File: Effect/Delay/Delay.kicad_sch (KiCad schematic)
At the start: 23 parts, among them J1 Conn_01x04_Pin, J2 Conn_01x03_Pin, U1 PT2399

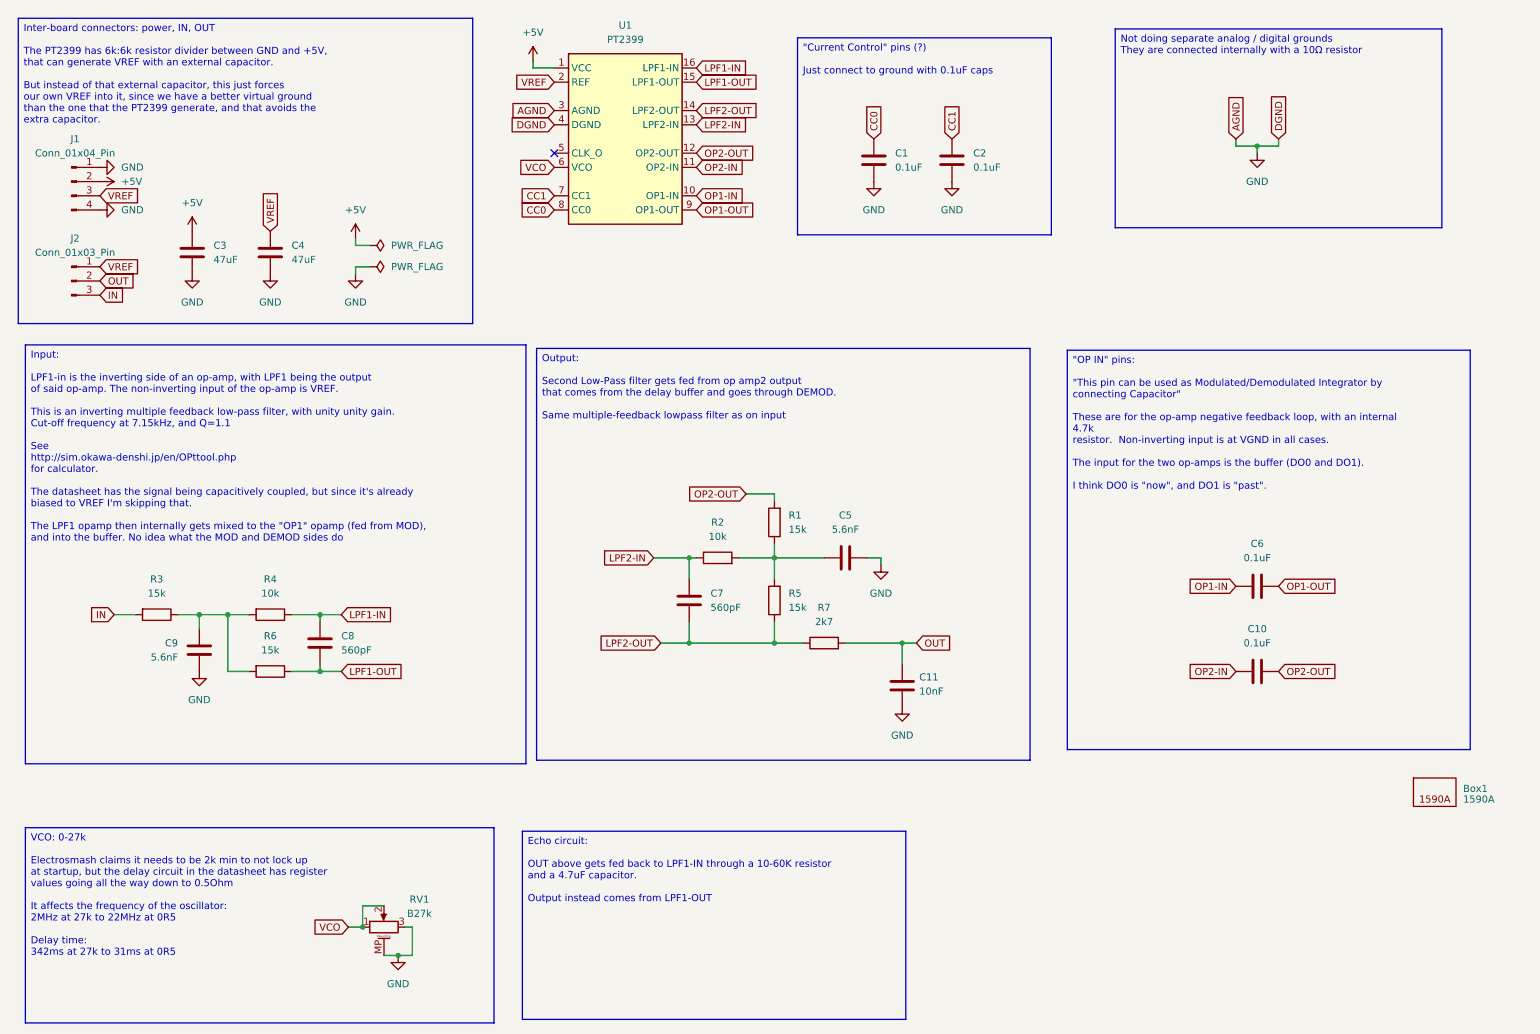
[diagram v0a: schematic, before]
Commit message: Turn the delay pedal into an echo
For testing, the delay pedal did a pure delayed output.  And it tests
fine, but I think what is more interesting to use is an actual echo
pedal where the delay gets fed back into the input.

Maybe it could have a mixed mode and do either? Or both? Anyway, this
just does the feedback thing.

Signed-off-by: Linus Torvalds <torvalds@linux-foundation.org>
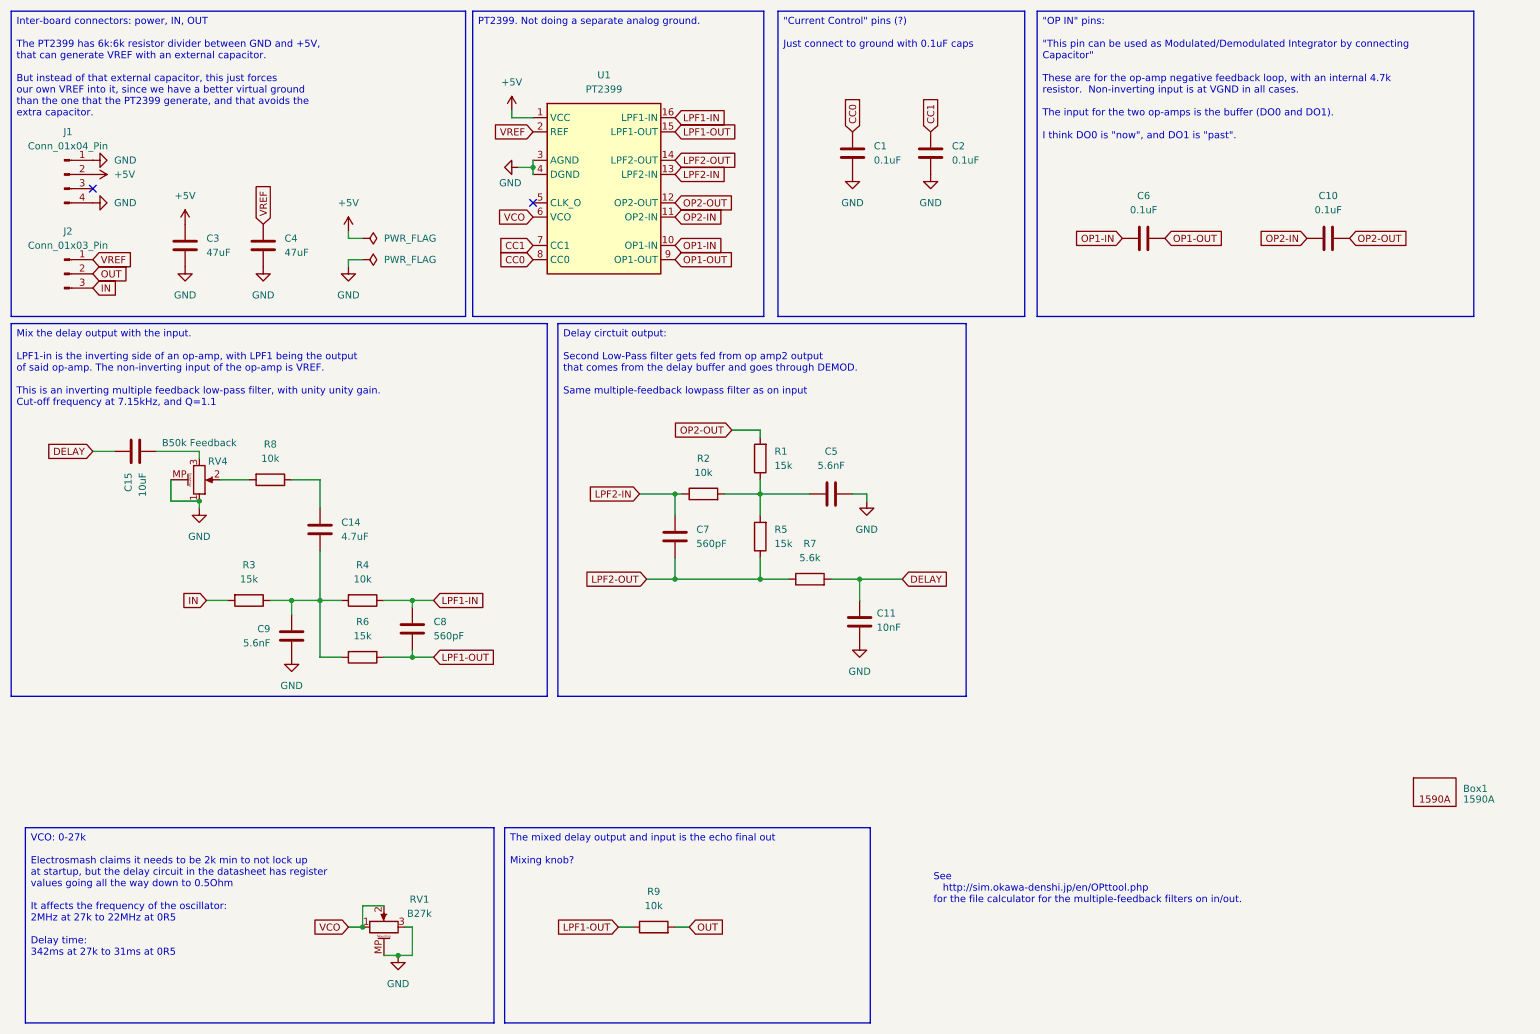
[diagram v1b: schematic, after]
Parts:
- added C14: 4.7uF, Capacitor_SMD:C_0805_2012Metric_Pad1.18x1.45mm_HandSolder, symbol Device:C
- added C15: 10uF, Capacitor_SMD:C_0805_2012Metric_Pad1.18x1.45mm_HandSolder, symbol Device:C
- added R8, R9: 10k, Resistor_SMD:R_0805_2012Metric_Pad1.20x1.40mm_HandSolder, symbol Device:R
- added RV4: B50k Feedback, Mylib:Potentiometer_9mm_MP, symbol Device:R_Potentiometer_MountingPin
- R7: value 2k7 -> 5.6k
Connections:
- net GND: now also RV4.1, RV4.MP (MountPin)
- net LPF1-OUT: now also R9.1
- net OUT: now also R9.2; no longer C11.2, R7.2
- net VREF: no longer J1.3 (Pin_3)
- net at C9.1, R3.1, R4.2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: now also C14.2
- new net: C15.2, RV4.3
- new net: C14.1, R8.1
- new net: R8.2, RV4.2
- new net DELAY: C11.2, C15.1, R7.2
- no-connect marks 1 -> 2
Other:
- note added: "See http://sim.okawa-denshi.jp/en/OPttool.php for the file calculator for the multiple-feedback filters on in/out."
- moved on the sheet: C1, C10, C11, C2, C3, C4, C5, C6, C7, C8, C9, J1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
